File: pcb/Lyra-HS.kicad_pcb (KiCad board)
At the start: 2 copper layers, 93 parts, among them J1 Computer/Power, J2 AVR-ISP-6, J3 AudioJack3, SW1 SW_Push, SW19 SW_Push, SW2 SW_Push, SW20 SW_Push, SW21 SW_Push, SW22 SW_Push, SW23 SW_Push, SW24 SW_Push, SW25 SW_Push, SW3 SW_Push, SW37 SW_Push, SW38 SW_Push, SW39 SW_Push, SW4 SW_Push, SW40 SW_Push, SW41 SW_Push, SW42 SW_Push, SW43 SW_Push, SW5 SW_Push, SW55 SW_Push, SW56 SW_Push, SW57 SW_Push, SW58 SW_Push, SW59 SW_Push, SW6 SW_Push, SW60 SW_Push, SW61 SW_Push, SW7 SW_Push, SW73 SW_Push, SW74 SW_Push, SW75 SW_Push, SW76 SW_Push, SW77 SW_Push, SW78 SW_Push, SW79 SW_Push, U1 ATmega32U4-MU, U2 SRV05-4

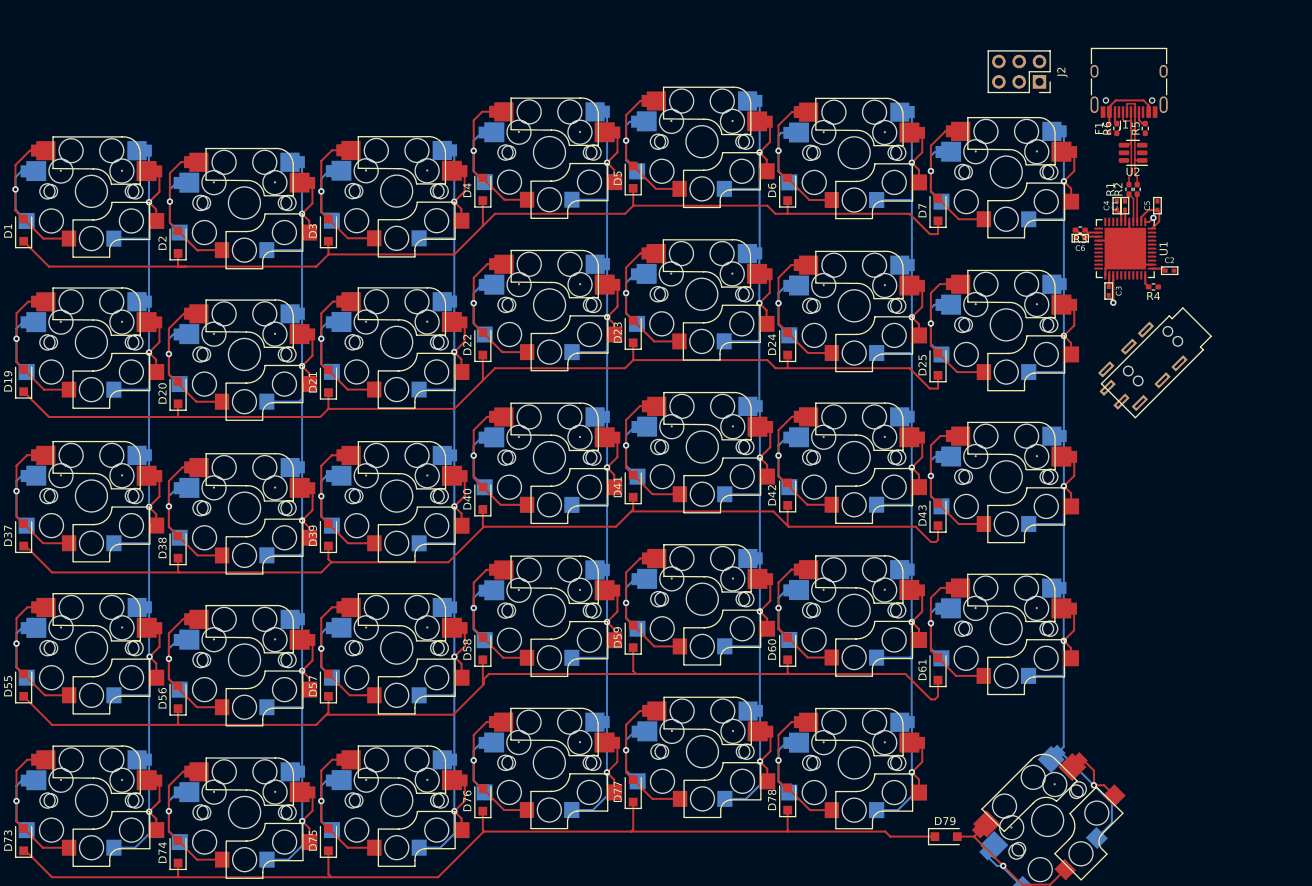
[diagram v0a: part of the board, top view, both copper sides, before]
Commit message: Initial MCU>Matrix hookup
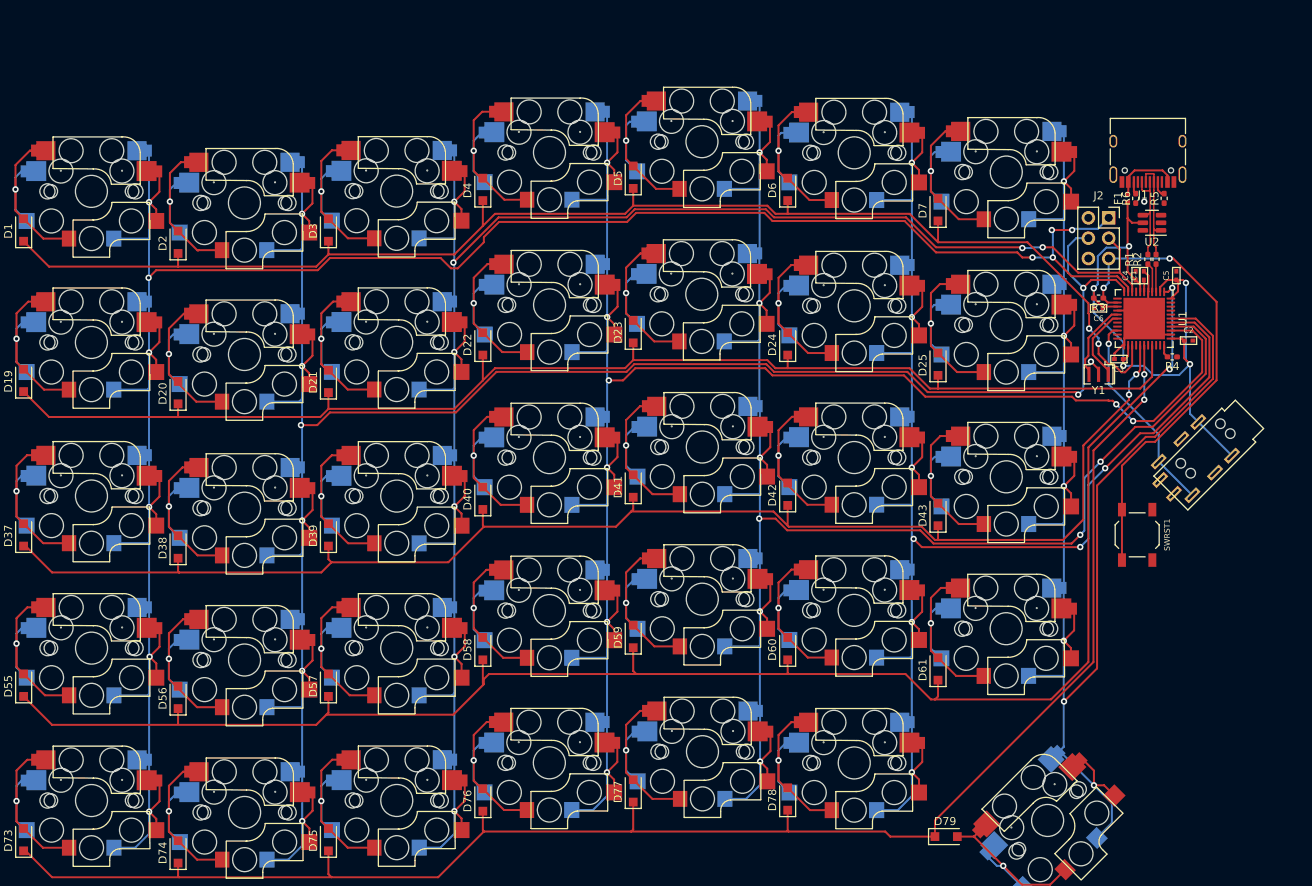
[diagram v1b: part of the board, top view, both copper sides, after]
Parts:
- added SWRST1: SW_Push, Keeb.io:SW_SPST_TL3342, F.Cu at (201.7, 102.6)
- added Y1: 16mhz, Crystal:Resonator_SMD_Murata_CSTxExxV-3Pin_3.0x1.1mm, F.Cu at (196.8, 82.5)
- moved J2 19.1 mm to (198.1, 63.0), turned to 0 degrees
- moved J3 13.3 mm to (214.4, 88.9)
- moved C6 9.06 mm to (196.8, 74.3)
- moved R4 9.05 mm to (206.1, 80.4)
- moved F1 9.05 mm to (200.5, 60.6)
- moved J1 9.05 mm to (203.0, 54.5)
- moved R1 9.05 mm to (203.0, 68.2)
- moved R2 9.05 mm to (204.0, 68.2)
- moved R5 9.05 mm to (205.1, 60.6)
- moved R6 9.05 mm to (201.5, 60.6)
- moved U2 9.05 mm to (203.5, 63.6)
- moved C1 9.05 mm to (202.5, 70.2)
- moved C2 9.05 mm to (208.1, 78.3)
- moved C4 9.05 mm to (201.5, 70.2)
- moved C5 9.05 mm to (206.6, 70.2)
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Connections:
- J3 pad A: (no net) -> unconnected-(J3-PadA)
- J3 pad B: (no net) -> VCC
- J3 pad C: (no net) -> GND
- J3 pad D: (no net) -> Serial
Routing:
- net COL0: track 143.9 -> 286.8 mm, vias 5 -> 10
- net COL1: track 144.1 -> 275.0 mm, vias 5 -> 8
- net COL2: track 143.9 -> 241.2 mm, vias 5 -> 8
- net COL3: track 144.0 -> 232.5 mm, vias 5 -> 8
- net COL4: track 144.0 -> 223.2 mm, vias 5 -> 8
- net VCC: track 14.1 -> 87.5 mm, vias 0 -> 5
- net ROW3: track 136.4 -> 208.6 mm, vias 1 -> 2
- net ROW4: track 132.3 -> 204.6 mm, vias 0 -> 2
- net COL5: track 144.0 -> 204.7 mm, vias 5 -> 8
- net COL6: track 146.9 -> 207.2 mm, vias 5 -> 6
- net RST: track 1.83 -> 60.8 mm, vias 0 -> 2
- net ROW2: track 133.1 -> 176.7 mm, vias 0 -> 2
- net ROW0: track 136.6 -> 170.4 mm, vias 1 -> 2
- net ROW1: track 132.3 -> 163.6 mm
- net Serial: track 0.00 -> 25.7 mm, vias 0 -> 1
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
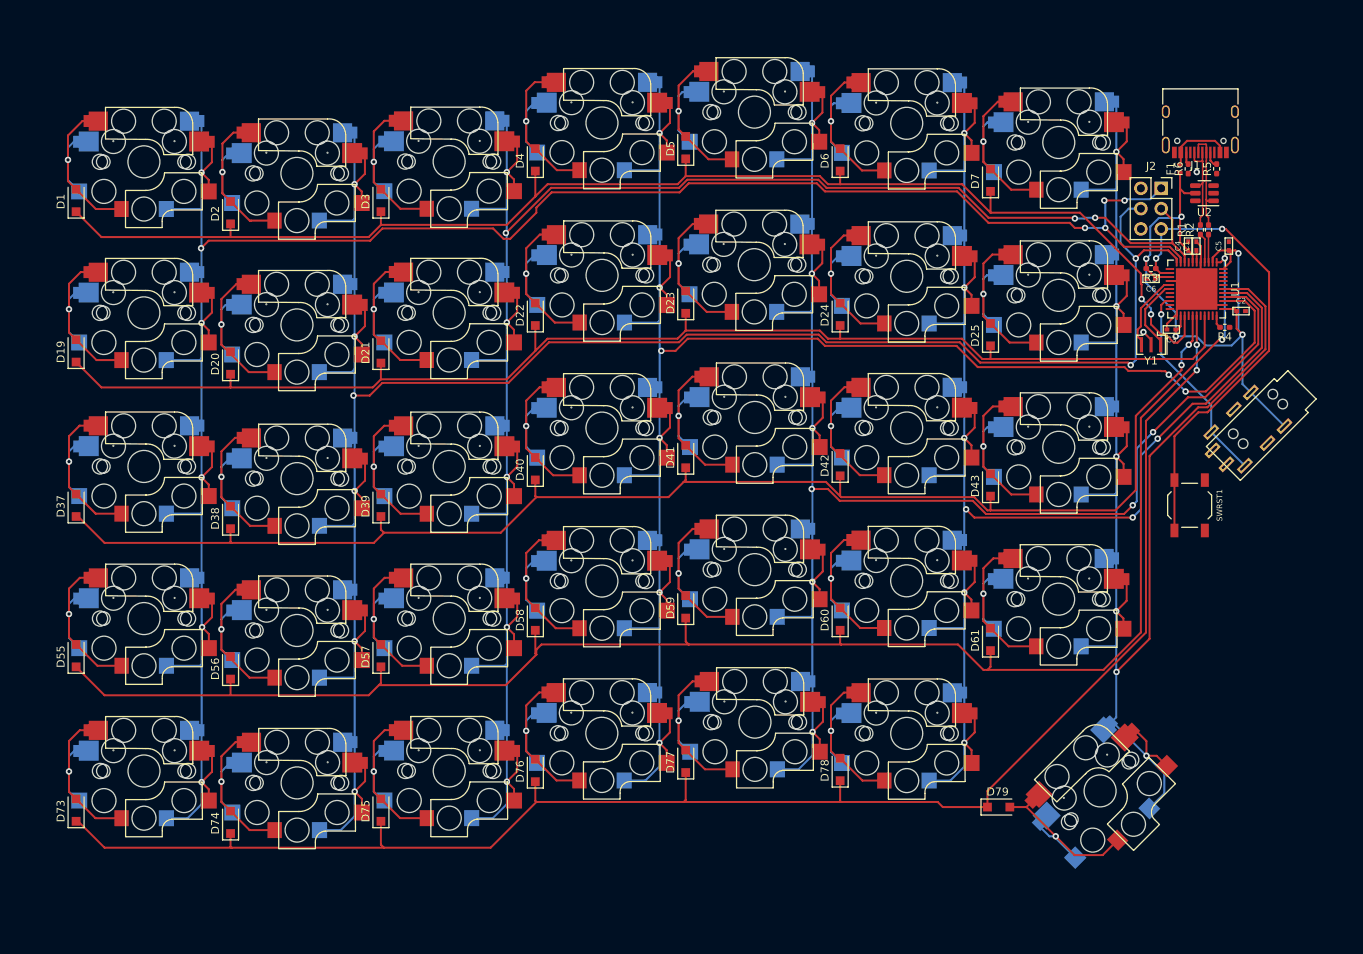
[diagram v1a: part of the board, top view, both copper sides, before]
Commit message: Initial Edge Cuts
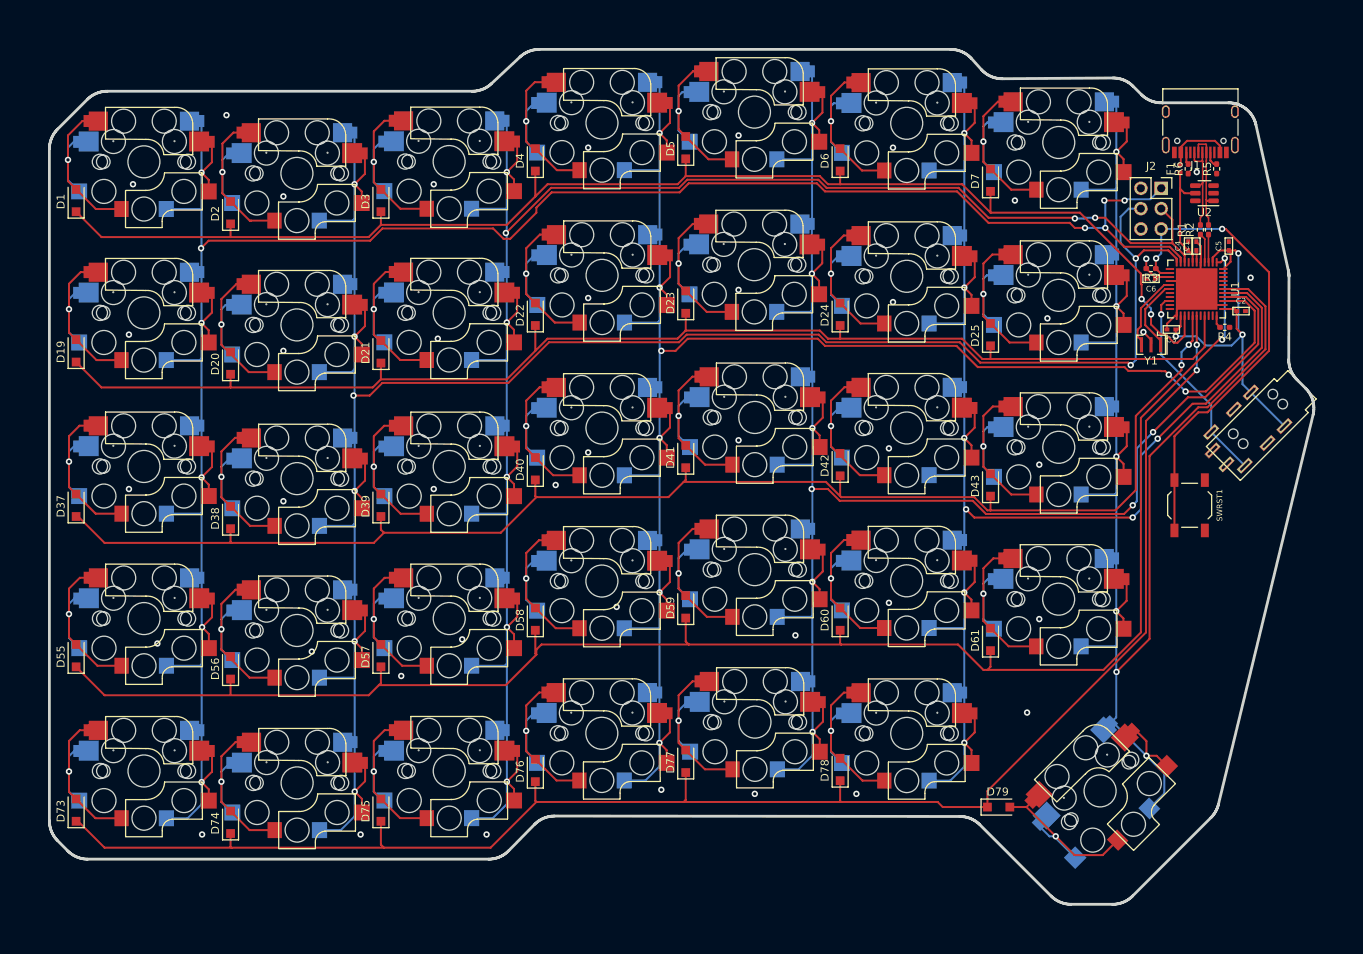
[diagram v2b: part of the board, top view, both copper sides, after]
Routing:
- net VCC: track 87.5 -> 67.6 mm, vias 5 -> 4
- net GND: vias 2 -> 41
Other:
- board outline added: 158.1 x 106.9 mm

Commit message: MCU area shenanigans
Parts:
- J3: footprint Lily58:TRRS_JACK_MJ4PP9 -> Keeb.io:TRRS-PJ-320A-Dual-Overlayed
- moved J2 52.0 mm to (199.4, 114.9), turned to 180 degrees
- moved Y1 6.38 mm to (196.2, 76.2), turned to 90 degrees
- moved J3 2.05 mm to (213.8, 86.9)
- moved SWRST1 1.67 mm to (200.0, 102.9)
- moved R3 0.76 mm to (197.3, 72.4)
- moved C6 0.64 mm to (196.8, 73.7)
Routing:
- net VCC: track 67.6 -> 117.4 mm, vias 4 -> 6
- net COL2: track 241.2 -> 285.2 mm, vias 8 -> 9
- net COL0: track 286.8 -> 325.4 mm, vias 10 -> 9
- net COL1: track 275.0 -> 300.9 mm, vias 8 -> 9
- net GND: track 23.0 -> 30.4 mm, vias 41 -> 57
- net Net-(U1-Pad16): track 9.76 -> 3.03 mm
- net ROW0: track 170.4 -> 176.1 mm
- net Net-(U1-Pad17): track 9.39 -> 4.17 mm
- net RST: track 60.8 -> 64.2 mm
- net ROW3: track 208.6 -> 210.5 mm
- net Serial: track 25.7 -> 24.2 mm
- net COL5: track 204.7 -> 203.8 mm
- net COL4: track 223.2 -> 222.2 mm
- net COL3: track 232.5 -> 231.7 mm
- net Net-(D56-Pad2): track 24.1 -> 23.5 mm
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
